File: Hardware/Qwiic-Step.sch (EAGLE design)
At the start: 56 parts, among them J1 PTH, J2 Qwiic Right Angle, J3 5.5x2.1mm Barrel, J4 Qwiic Right Angle, J5 ISP, U1 A4988ALT1, U2 ATMEGA328P_TQFP, Y1 16MHz

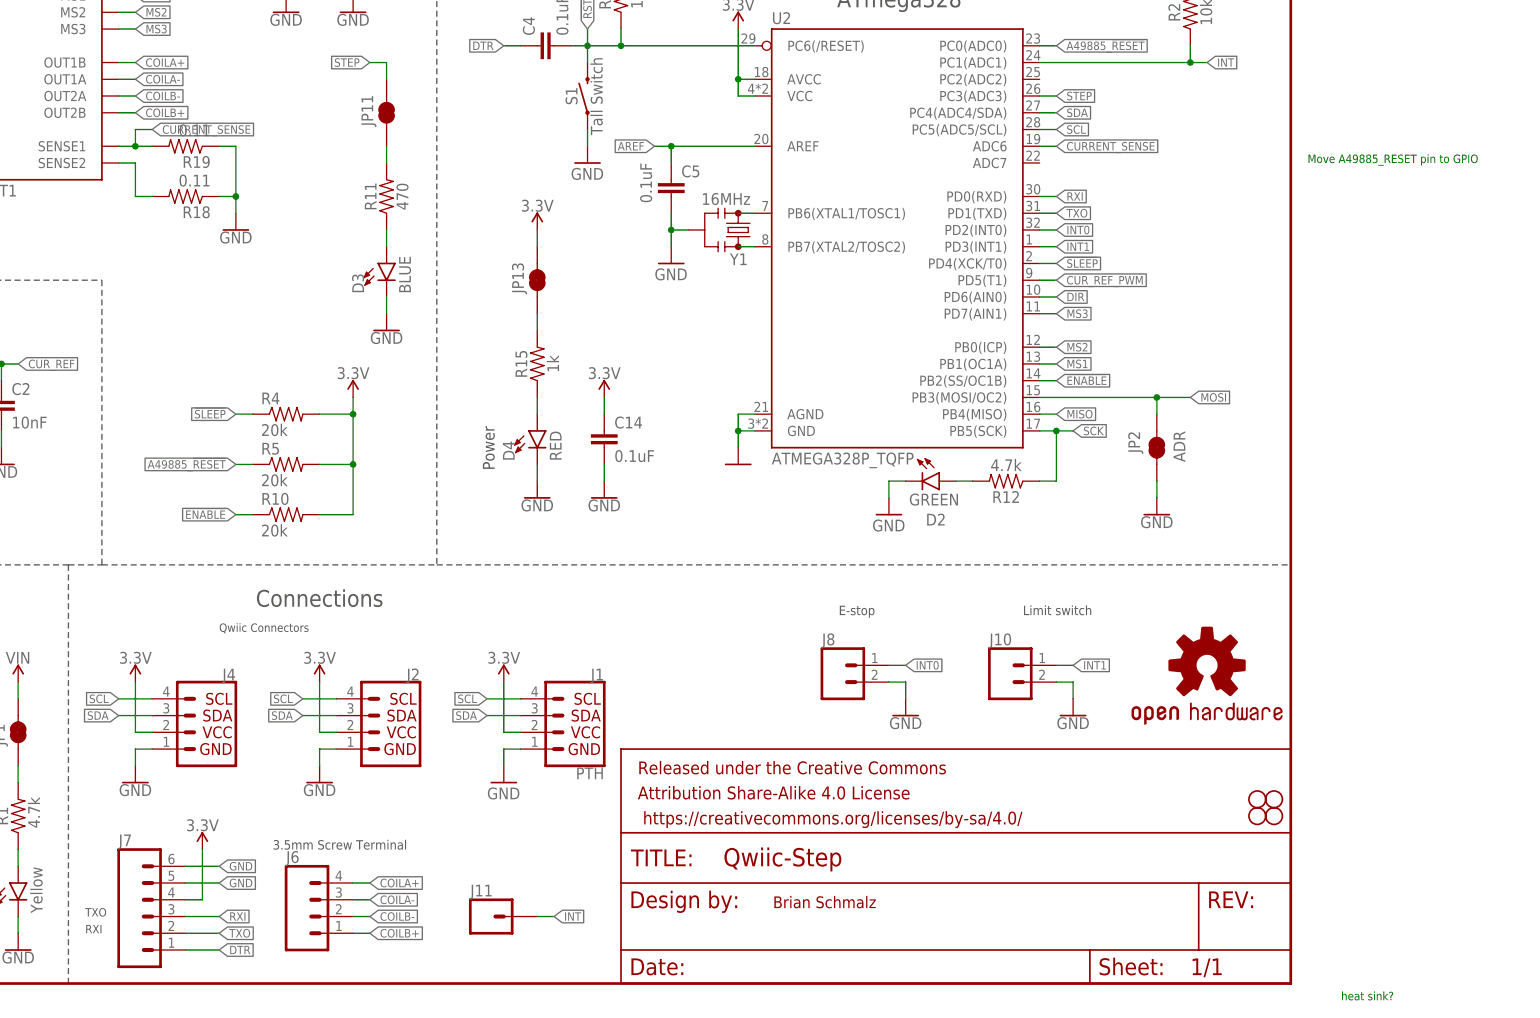
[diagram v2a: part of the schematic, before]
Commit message: Cleaning up Rev 1 changes. Still need to connect current sense trace, run DRC.
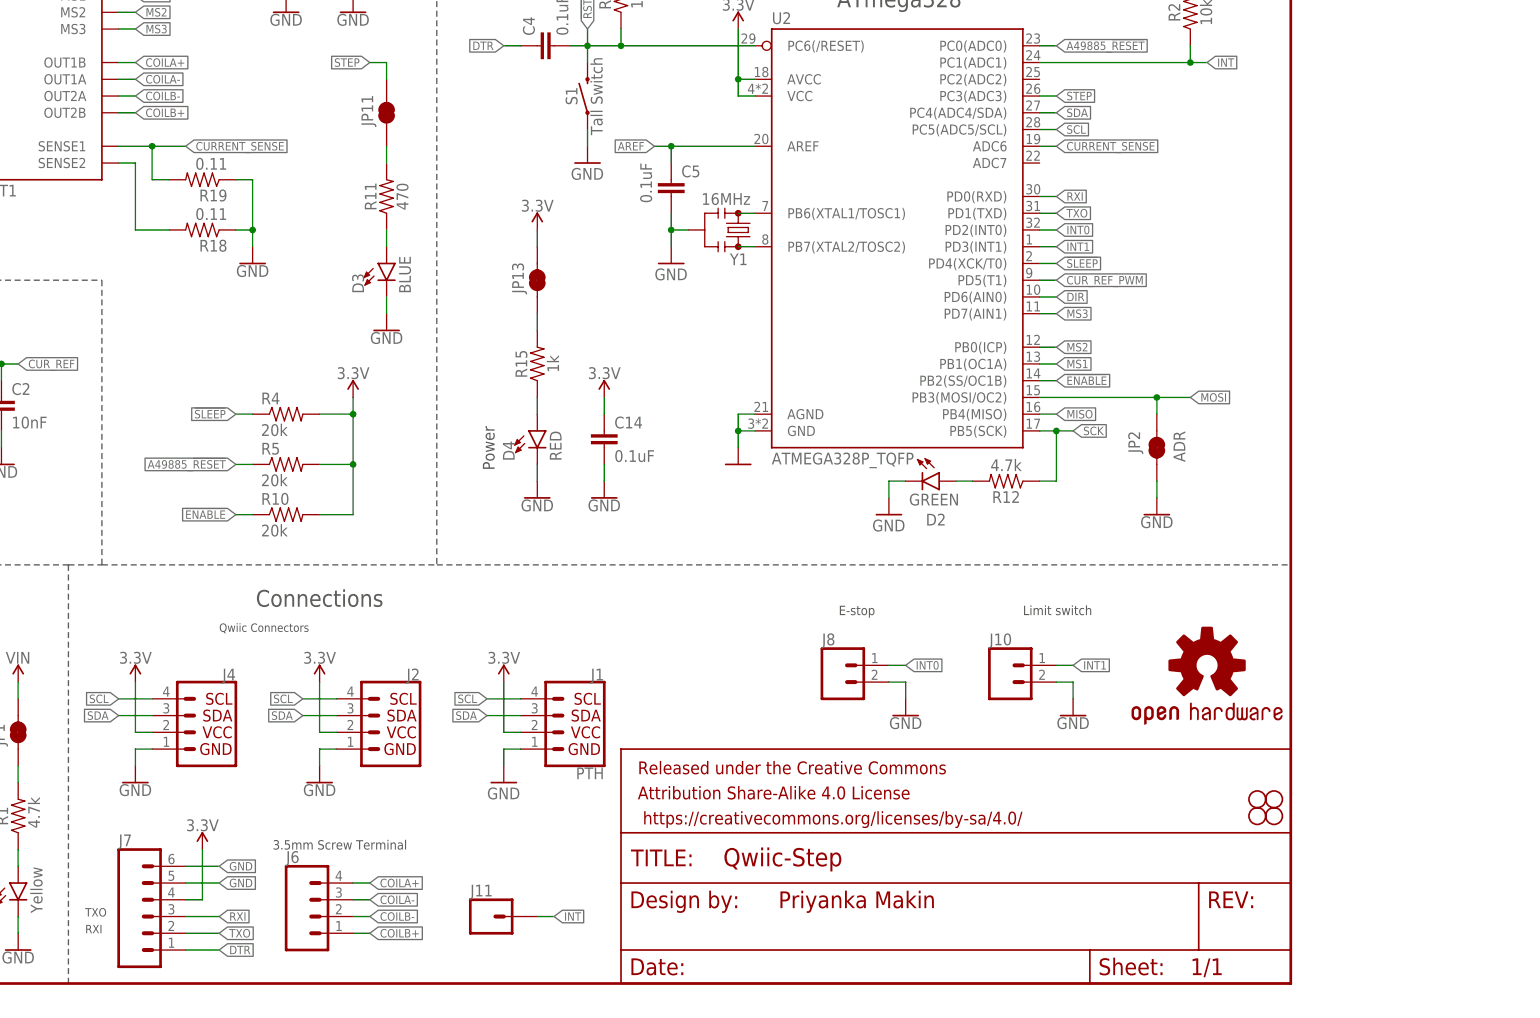
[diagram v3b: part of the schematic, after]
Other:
- note added: "Priyanka Makin"
- note removed: "Brian Schmalz"
- note removed: "Move A49885_RESET pin to GPIO"
- note removed: "heat sink?"
- moved on the sheet: R18, R19
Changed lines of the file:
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@@
 <sheet>
 <plain>
-<text x="169.672" y="11.43" size="1.778" layer="94"> Brian Schmalz</text>
 <text x="2.54" y="33.02" size="1.4224" layer="97">8 to 35V DC</text>
 <text x="2.286" y="68.58" size="1.4224" layer="97">Current pot adjusts max coil current:
@@
 <text x="180.34" y="55.88" size="1.4224" layer="97">E-stop</text>
 <text x="2.54" y="20.32" size="1.4224" layer="97">3.5mm Screw Terminal</text>
-<text x="256.54" y="-2.54" size="1.27" layer="91">heat sink?</text>
-<text x="251.46" y="124.46" size="1.27" layer="91">Move A49885_RESET pin to GPIO</text>
+<text x="171.196" y="11.43" size="2.54" layer="94">Priyanka Makin</text>
 </plain>
 <instances>
@@
 <instance part="JP8" gate="G$1" x="243.84" y="25.4" smashed="yes"/>
 <instance part="JP9" gate="G$1" x="246.38" y="25.4" smashed="yes"/>
-<instance part="R18" gate="G$1" x="81.28" y="119.38" smashed="yes" rot="R180">
-<attribute name="NAME" x="85.09" y="117.8814" size="1.778" layer="95" rot="R180"/>
-<attribute name="VALUE" x="85.09" y="122.682" size="1.778" layer="96" rot="R180"/>
-</instance>
-<instance part="R19" gate="G$1" x="81.28" y="127" smashed="yes" rot="R180">
-<attribute name="NAME" x="85.09" y="125.5014" size="1.778" layer="95" rot="R180"/>
-<attribute name="VALUE" x="85.09" y="130.302" size="1.778" layer="96" rot="R180"/>
+<instance part="R18" gate="G$1" x="83.82" y="114.3" smashed="yes" rot="R180">
+<attribute name="NAME" x="87.63" y="112.8014" size="1.778" layer="95" rot="R180"/>
+<attribute name="VALUE" x="87.63" y="117.602" size="1.778" layer="96" rot="R180"/>
+</instance>
+<instance part="R19" gate="G$1" x="83.82" y="121.92" smashed="yes" rot="R180">
+<attribute name="NAME" x="87.63" y="120.4214" size="1.778" layer="95" rot="R180"/>
+<attribute name="VALUE" x="87.63" y="125.222" size="1.778" layer="96" rot="R180"/>
 </instance>
 <instance part="R20" gate="G$1" x="25.4" y="121.92" smashed="yes" rot="MR270">
@@
 <attribute name="VALUE" x="25.4" y="111.506" size="1.778" layer="96" rot="MR0" align="top-center"/>
 </instance>
-<instance part="GND15" gate="1" x="88.9" y="114.3" smashed="yes">
-<attribute name="VALUE" x="88.9" y="114.046" size="1.778" layer="96" align="top-center"/>
+<instance part="GND15" gate="1" x="91.44" y="109.22" smashed="yes">
+<attribute name="VALUE" x="91.44" y="108.966" size="1.778" layer="96" align="top-center"/>
 </instance>
 <instance part="GND26" gate="1" x="40.64" y="27.94" smashed="yes">
@@
 </segment>
 <segment>
-<wire x1="86.36" y1="119.38" x2="88.9" y2="119.38" width="0.1524" layer="91"/>
-<wire x1="88.9" y1="119.38" x2="88.9" y2="116.84" width="0.1524" layer="91"/>
-<wire x1="86.36" y1="127" x2="88.9" y2="127" width="0.1524" layer="91"/>
-<wire x1="88.9" y1="127" x2="88.9" y2="119.38" width="0.1524" layer="91"/>
-<junction x="88.9" y="119.38"/>
+<wire x1="88.9" y1="114.3" x2="91.44" y2="114.3" width="0.1524" layer="91"/>
+<wire x1="91.44" y1="114.3" x2="91.44" y2="111.76" width="0.1524" layer="91"/>
+<wire x1="88.9" y1="121.92" x2="91.44" y2="121.92" width="0.1524" layer="91"/>
+<wire x1="91.44" y1="121.92" x2="91.44" y2="114.3" width="0.1524" layer="91"/>
+<junction x="91.44" y="114.3"/>
 <pinref part="R18" gate="G$1" pin="1"/>
 <pinref part="R19" gate="G$1" pin="1"/>
@@
 <segment>
 <wire x1="71.12" y1="124.46" x2="73.66" y2="124.46" width="0.1524" layer="91"/>
+<pinref part="U1" gate="G$1" pin="SENSE2"/>
+<wire x1="73.66" y1="124.46" x2="73.66" y2="114.3" width="0.1524" layer="91"/>
 <pinref part="R18" gate="G$1" pin="2"/>
-<wire x1="73.66" y1="124.46" x2="73.66" y2="119.38" width="0.1524" layer="91"/>
-<wire x1="73.66" y1="119.38" x2="76.2" y2="119.38" width="0.1524" layer="91"/>
-<pinref part="U1" gate="G$1" pin="SENSE2"/>
+<wire x1="73.66" y1="114.3" x2="78.74" y2="114.3" width="0.1524" layer="91"/>
 </segment>
 </net>
 <net name="CURRENT_SENSE" class="0">
 <segment>
-<wire x1="71.12" y1="127" x2="73.66" y2="127" width="0.1524" layer="91"/>
+<pinref part="U1" gate="G$1" pin="SENSE1"/>
+<wire x1="71.12" y1="127" x2="76.2" y2="127" width="0.1524" layer="91"/>
+<label x="81.28" y="127" size="1.27" layer="95" xref="yes"/>
 <pinref part="R19" gate="G$1" pin="2"/>
-<pinref part="U1" gate="G$1" pin="SENSE1"/>
-<wire x1="73.66" y1="127" x2="76.2" y2="127" width="0.1524" layer="91"/>
-<wire x1="73.66" y1="127" x2="73.66" y2="129.54" width="0.1524" layer="91"/>
-<junction x="73.66" y="127"/>
-<wire x1="73.66" y1="129.54" x2="76.2" y2="129.54" width="0.1524" layer="91"/>
-<label x="76.2" y="129.54" size="1.27" layer="95" xref="yes"/>
-</segment>
-<segment>
+<wire x1="76.2" y1="127" x2="81.28" y2="127" width="0.1524" layer="91"/>
+<wire x1="78.74" y1="121.92" x2="76.2" y2="121.92" width="0.1524" layer="91"/>
+<wire x1="76.2" y1="121.92" x2="76.2" y2="127" width="0.1524" layer="91"/>
+<junction x="76.2" y="127"/>
+</segment>
+<segment>

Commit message: Update Qwiic-Step.sch
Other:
- note added: "External Interrupt Pin"
- note added: "Latch Terminal"
- note added: "Programming"
- note removed: "3.5mm Screw Terminal"
- note removed: "Current pot adjusts max coil current: Full clockwise = 2.08A coil current Note driver can only output 2A coil current, and is dependent on input voltage, motor, and heat sinking/fan to reach this."
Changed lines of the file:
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@@
 <plain>
 <text x="2.54" y="33.02" size="1.4224" layer="97">8 to 35V DC</text>
-<text x="2.286" y="68.58" size="1.4224" layer="97">Current pot adjusts max coil current:
-Full clockwise = 2.08A coil current
-Note driver can only output 2A coil current,
-and is dependent on input voltage, motor,
-and heat sinking/fan to reach this.</text>
-<text x="94.488" y="20.32" size="1.4224" layer="97">3.5mm Screw Terminal</text>
+<text x="99.568" y="22.86" size="1.4224" layer="97">Latch Terminal</text>
 <text x="58.42" y="177.8" size="2.54" layer="97" align="center">Stepper Driver</text>
 <text x="101.6" y="58.42" size="2.54" layer="97" align="center">Connections</text>
@@
 <text x="66.04" y="10.16" size="1.27" layer="97">TXO</text>
 <text x="66.04" y="7.62" size="1.27" layer="97">RXI</text>
-<text x="86.36" y="53.34" size="1.27" layer="97">Qwiic Connectors</text>
 <text x="208.28" y="55.88" size="1.4224" layer="97">Limit switch</text>
 <text x="180.34" y="55.88" size="1.4224" layer="97">E-stop</text>
-<text x="2.54" y="20.32" size="1.4224" layer="97">3.5mm Screw Terminal</text>
 <text x="171.196" y="11.43" size="2.54" layer="94">Priyanka Makin</text>
+<text x="119.888" y="17.78" size="1.4224" layer="97">External Interrupt Pin</text>
+<text x="99.568" y="22.86" size="1.4224" layer="97">Latch Terminal</text>
+<text x="99.568" y="22.86" size="1.4224" layer="97">Latch Terminal</text>
+<text x="74.168" y="25.4" size="1.4224" layer="97">Programming</text>
+<text x="86.868" y="53.34" size="1.4224" layer="97">Qwiic Connectors</text>
+<text x="3.048" y="20.32" size="1.4224" layer="97">Latch Terminal</text>
 </plain>
 <instances>
@@
 </drawing>
 <compatibility>
-<note version="6.3" minversion="6.2.2" severity="warning">
-Since Version 6.2.2 text objects can contain more than one line,
-which will not be processed correctly with this version.
-</note>
 <note version="8.3" severity="warning">
 Since Version 8.3, EAGLE supports URNs for individual library

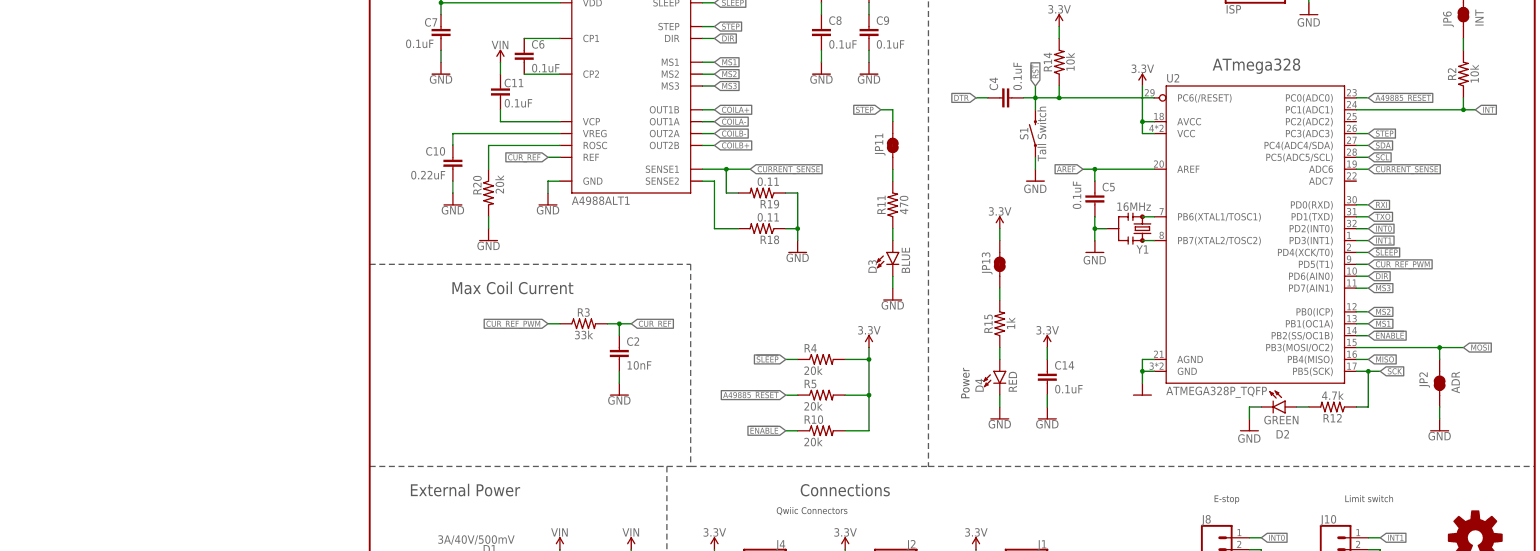
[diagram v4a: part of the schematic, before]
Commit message: Added amplifier circuit to current sense reading
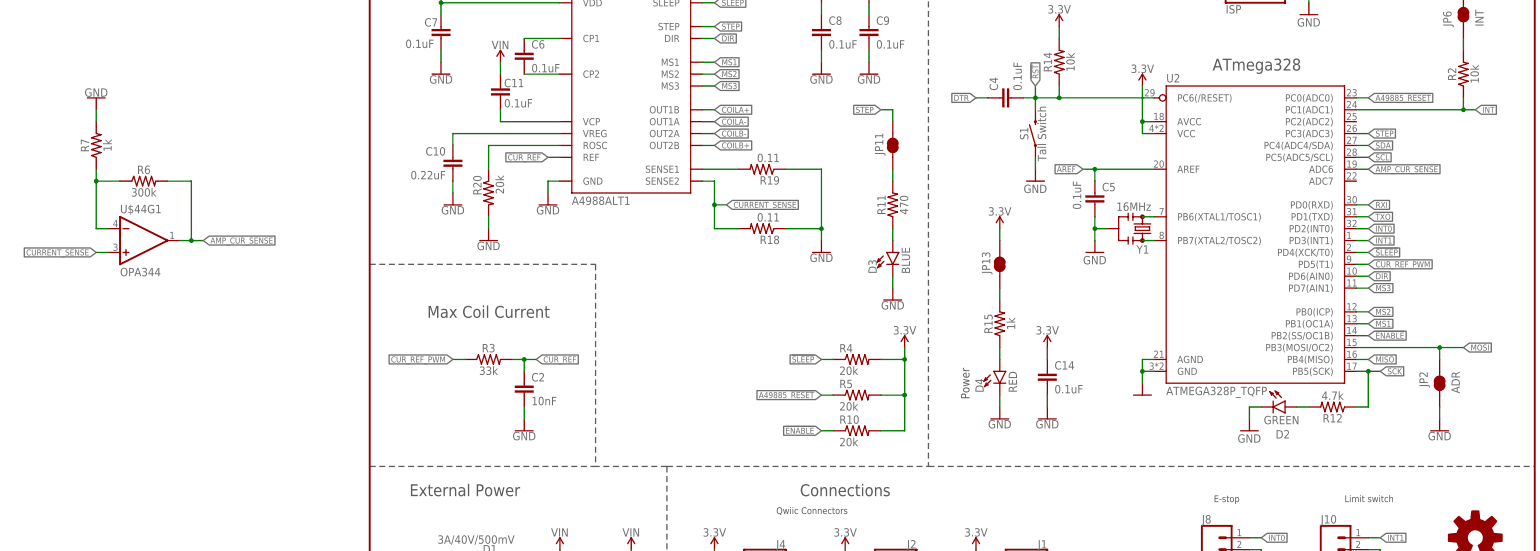
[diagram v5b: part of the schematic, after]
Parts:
- added R6: 300k, SparkFun-Resistors:300KOHM-0603-1/10W-1%
- added R7: 1k, SparkFun-Resistors:1KOHM-0603-1/10W-1%
- added U$44: OPA344, SparkFun-IC-Amplifiers:OPA344
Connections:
- removed net N$31: R18.2, U1.SENSE2
- new net AMP_CUR_SENSE: R6.2, U$44G1.OUT, U2.ADC6
- new net N$2: R6.1, R7.1, U$44G1.-IN
- new net N$3: R19.2, U1.SENSE1
- net CURRENT_SENSE: now also R18.2, U$44G1.+IN, U1.SENSE2; no longer R19.2, U1.SENSE1, U2.ADC6
- net GND: now also R7.2
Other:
- moved on the sheet: C2, R10, R19, R3, R4, R5
